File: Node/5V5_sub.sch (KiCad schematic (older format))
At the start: 21 parts, among them U501 TPS54361

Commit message: Generated BOM, filled out part numbers for precision resistors and headers.
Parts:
- R505: MFG. P/N (none) -> RC0805FR-0766K5L; Manufacturer (none) -> Yageo; Vendor (none) -> DigiKey; Vendor P/N (none) -> 311-66.5KCRCT-ND
- R508: MFG. P/N (none) -> RC0805FR-0711K3L; Manufacturer (none) -> Yageo; Vendor (none) -> DigiKey; Vendor P/N (none) -> 311-11.3KCRCT-ND
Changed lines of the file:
@@
 EESchema Schematic File Version 2
 LIBS:hyper_capstone
+LIBS:Connector
 LIBS:node-cache
 EELAYER 25 0
@@
 	3350 4650 3350 4850
 $Comp
-L GND #PWR510
+L GND #PWR034
 U 1 1 59F1BBFD
 P 3350 4850
-F 0 "#PWR510" H 3350 4600 60  0001 C CNN
+F 0 "#PWR034" H 3350 4600 60  0001 C CNN
 F 1 "GND" H 3350 4700 60  0000 C CNN
 F 2 "" H 3350 4850 60  0000 C CNN
@@
 	2850 4500 2850 4850
 $Comp
-L GND #PWR509
+L GND #PWR035
 U 1 1 59F1BC04
 P 2850 4850
-F 0 "#PWR509" H 2850 4600 60  0001 C CNN
+F 0 "#PWR035" H 2850 4600 60  0001 C CNN
 F 1 "GND" H 2850 4700 60  0000 C CNN
 F 2 "" H 2850 4850 60  0000 C CNN
@@
 Connection ~ 3800 5750
 $Comp
-L GND #PWR513
+L GND #PWR036
 U 1 1 59F1BC0B
 P 3800 5800
-F 0 "#PWR513" H 3800 5550 60  0001 C CNN
+F 0 "#PWR036" H 3800 5550 60  0001 C CNN
 F 1 "GND" H 3800 5650 60  0000 C CNN
 F 2 "" H 3800 5800 60  0000 C CNN
@@
 	5750 4300 5750 4450
 $Comp
-L GND #PWR502
+L GND #PWR037
 U 1 1 59F1BC3A
 P 5750 4450
-F 0 "#PWR502" H 5750 4200 60  0001 C CNN
+F 0 "#PWR037" H 5750 4200 60  0001 C CNN
 F 1 "GND" H 5750 4300 60  0000 C CNN
 F 2 "" H 5750 4450 60  0000 C CNN
@@
 	6250 4600 6250 4700
 $Comp
-L GND #PWR504
+L GND #PWR038
 U 1 1 59F1BC42
 P 6250 4700
-F 0 "#PWR504" H 6250 4450 60  0001 C CNN
+F 0 "#PWR038" H 6250 4450 60  0001 C CNN
 F 1 "GND" H 6250 4550 60  0000 C CNN
 F 2 "" H 6250 4700 60  0000 C CNN
@@
 F 2 "Resistors_SMD:R_0805_HandSoldering" V 7180 3950 30  0001 C CNN
 F 3 "" H 7250 3950 30  0000 C CNN
-F 4 "ERJ-6ENF6652V" H 7250 3950 60  0001 C CNN "Mfg. Part Num"
-F 5 "Panasonic" H 7250 3950 60  0001 C CNN "Mfg. Name"
-F 6 "P66.5KCCT-ND" H 7250 3950 60  0001 C CNN "Vendor Part Num"
-F 7 "Digi-Key" H 7250 3950 60  0001 C CNN "Vendor Name"
+F 4 "Yageo" H 7250 3950 60  0001 C CNN "Manufacturer"
+F 5 "RC0805FR-0766K5L" H 7250 3950 60  0001 C CNN "MFG. P/N"
+F 6 "DigiKey" H 7250 3950 60  0001 C CNN "Vendor"
+F 7 "311-66.5KCRCT-ND" H 7250 3950 60  0001 C CNN "Vendor P/N"
 F 8 "1%" H 7400 3900 60  0000 C CNN "Tolerance"
+F 9 "ERJ-6ENF6652V" H 7250 3950 60  0001 C CNN "Mfg. Part Num"
+F 10 "Panasonic" H 7250 3950 60  0001 C CNN "Mfg. Name"
+F 11 "P66.5KCCT-ND" H 7250 3950 60  0001 C CNN "Vendor Part Num"
+F 12 "Digi-Key" H 7250 3950 60  0001 C CNN "Vendor Name"
 	1    7250 3950
 	1    0    0    -1
@@
 Connection ~ 7250 4300
 $Comp
-L GND #PWR512
+L GND #PWR039
 U 1 1 59F1BC5A
 P 7250 5000
-F 0 "#PWR512" H 7250 4750 60  0001 C CNN
+F 0 "#PWR039" H 7250 4750 60  0001 C CNN
 F 1 "GND" H 7250 4850 60  0000 C CNN
 F 2 "" H 7250 5000 60  0000 C CNN
@@
 	7850 4100 7850 4250
 $Comp
-L GND #PWR501
+L GND #PWR040
 U 1 1 59F1BC6E
 P 7850 4250
-F 0 "#PWR501" H 7850 4000 60  0001 C CNN
+F 0 "#PWR040" H 7850 4000 60  0001 C CNN
 F 1 "GND" H 7850 4100 60  0000 C CNN
 F 2 "" H 7850 4250 60  0000 C CNN
@@
 	4900 4600 4900 4700
 $Comp
-L GND #PWR503
+L GND #PWR041
 U 1 1 59F1BC77
 P 4900 4700
-F 0 "#PWR503" H 4900 4450 60  0001 C CNN
+F 0 "#PWR041" H 4900 4450 60  0001 C CNN
 F 1 "GND" H 4900 4550 60  0000 C CNN
 F 2 "" H 4900 4700 60  0000 C CNN
@@
 	1950 4050 1950 4800
 $Comp
-L GND #PWR507
+L GND #PWR042
 U 1 1 59F1BC9B
 P 1950 4800
-F 0 "#PWR507" H 1950 4550 60  0001 C CNN
+F 0 "#PWR042" H 1950 4550 60  0001 C CNN
 F 1 "GND" H 1950 4650 60  0000 C CNN
 F 2 "" H 1950 4800 60  0000 C CNN
@@
 	9700 4400 9700 4700
 $Comp
-L GND #PWR506
+L GND #PWR043
 U 1 1 59F1BCD5
 P 9700 4700
-F 0 "#PWR506" H 9700 4450 60  0001 C CNN
+F 0 "#PWR043" H 9700 4450 60  0001 C CNN
 F 1 "GND" H 9700 4550 60  0000 C CNN
 F 2 "" H 9700 4700 60  0000 C CNN
@@
 	10350 4100 10350 4250
 $Comp
-L GND #PWR511
+L GND #PWR044
 U 1 1 59F1BCE0
 P 10350 4850
-F 0 "#PWR511" H 10350 4600 60  0001 C CNN
+F 0 "#PWR044" H 10350 4600 60  0001 C CNN
 F 1 "GND" H 10350 4700 60  0000 C CNN
 F 2 "" H 10350 4850 60  0000 C CNN
@@
 	2350 4050 2350 4800
 $Comp
-L GND #PWR508
+L GND #PWR045
 U 1 1 59F1CBAA
 P 2350 4800
-F 0 "#PWR508" H 2350 4550 60  0001 C CNN
+F 0 "#PWR045" H 2350 4550 60  0001 C CNN
 F 1 "GND" H 2350 4650 60  0000 C CNN
 F 2 "" H 2350 4800 60  0000 C CNN
@@
 F 2 "Resistors_SMD:R_0805_HandSoldering" V 7180 4650 30  0001 C CNN
 F 3 "" H 7250 4650 30  0000 C CNN
-F 4 "Digi-Key" H 7250 4650 60  0001 C CNN "Vendor Name"
-F 5 "1%" H 7400 4600 60  0000 C CNN "Tolerance"
+F 4 "Yageo" H 7250 4650 60  0001 C CNN "Manufacturer"
+F 5 "RC0805FR-0711K3L" H 7250 4650 60  0001 C CNN "MFG. P/N"
+F 6 "DigiKey" H 7250 4650 60  0001 C CNN "Vendor"
+F 7 "311-11.3KCRCT-ND" H 7250 4650 60  0001 C CNN "Vendor P/N"
+F 8 "1%" H 7400 4600 60  0000 C CNN "Tolerance"
+F 9 "Digi-Key" H 7250 4650 60  0001 C CNN "Vendor Name"
 	1    7250 4650
 	1    0    0    -1
@@
 	9200 4350 9200 4700
 $Comp
-L GND #PWR505
+L GND #PWR046
 U 1 1 5A1A8A0F
 P 9200 4700
-F 0 "#PWR505" H 9200 4450 60  0001 C CNN
+F 0 "#PWR046" H 9200 4450 60  0001 C CNN
 F 1 "GND" H 9200 4550 60  0000 C CNN
 F 2 "" H 9200 4700 60  0000 C CNN

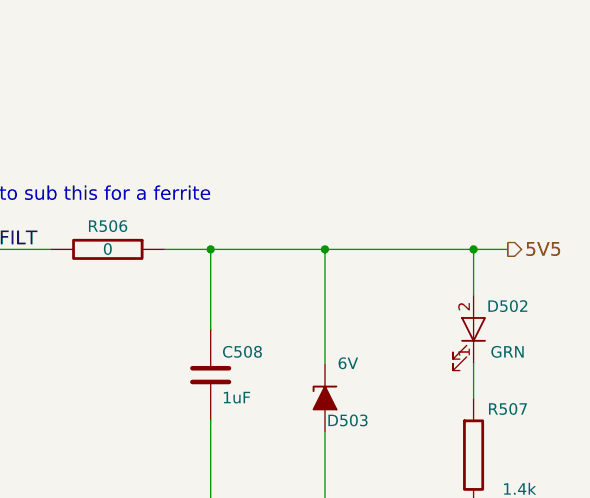
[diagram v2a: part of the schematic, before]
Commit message: Added testpoints and silkscreen descriptions to PCB. Added Paradigm template to schematic.
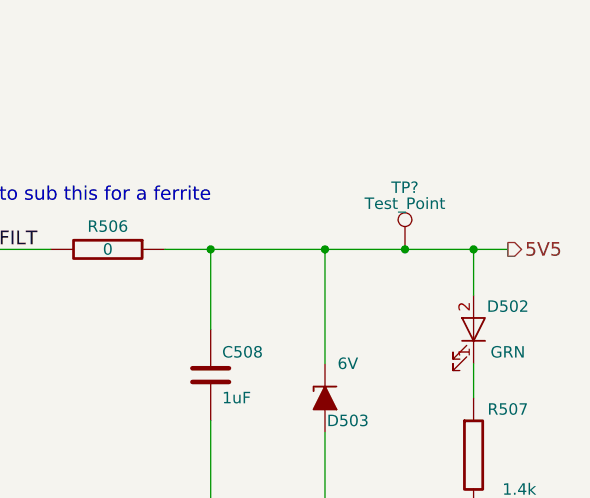
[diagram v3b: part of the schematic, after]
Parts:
- added TP?: Test_Point, Measurement_Points:Test_Point_Keystone_5000-5004_Miniature, symbol Test_Point
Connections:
- net 5V5: now also TP?.1
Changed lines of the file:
@@
 encoding utf-8
 Sheet 5 22
-Title ""
+Title "Node Board"
 Date ""
-Rev ""
+Rev "Rev 1.0"
 Comp ""
 Comment1 ""
@@
 Text Label 3550 2700 0    60   ~ 0
 ENABLE
+$Comp
+L Test_Point TP?
+U 1 1 5A71E940
+P 10050 3600
+F 0 "TP?" H 10050 3870 50  0000 C CNN
+F 1 "Test_Point" H 10050 3800 50  0000 C CNN
+F 2 "Measurement_Points:Test_Point_Keystone_5000-5004_Miniature" H 10250 3600 50  0001 C CNN
+F 3 "" H 10250 3600 50  0001 C CNN
+F 4 "Keystone Electronics" H 10050 3600 60  0001 C CNN "Manufacturer"
+F 5 "5000" H 10050 3600 60  0001 C CNN "Manufacturer P/N"
+F 6 "DigiKey" H 10050 3600 60  0001 C CNN "Vendor"
+F 7 "36-5000-ND" H 10050 3600 60  0001 C CNN "Vendor P/N"
+	1    10050 3600
+	1    0    0    -1
+$EndComp
+Connection ~ 10050 3600
 $EndSCHEMATC

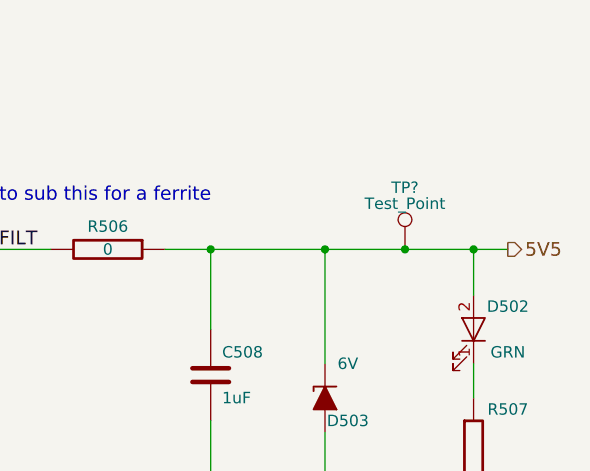
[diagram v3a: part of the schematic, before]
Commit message: fixed and routed driver spi issue
Added new rx/tx bus for solenoid driver. Routed it too. Nice.
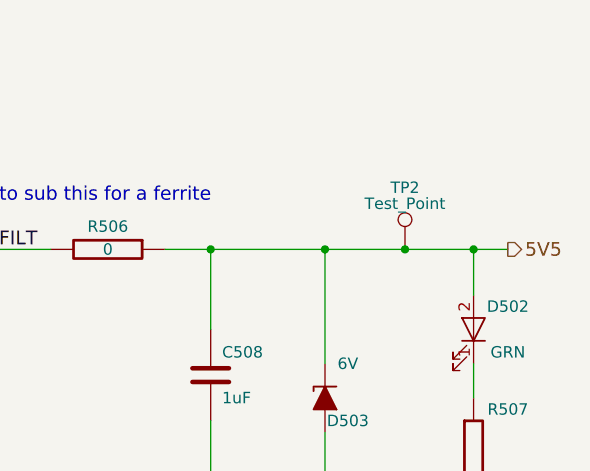
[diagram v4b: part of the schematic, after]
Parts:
- gave numbers to parts that had none: 1
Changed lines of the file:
@@
 EESchema Schematic File Version 2
 LIBS:hyper_capstone
-LIBS:Connector
 LIBS:node-cache
 EELAYER 25 0
@@
 ENABLE
 $Comp
-L Test_Point TP?
+L Test_Point TP2
 U 1 1 5A71E940
 P 10050 3600
-F 0 "TP?" H 10050 3870 50  0000 C CNN
+F 0 "TP2" H 10050 3870 50  0000 C CNN
 F 1 "Test_Point" H 10050 3800 50  0000 C CNN
 F 2 "Measurement_Points:Test_Point_Keystone_5000-5004_Miniature" H 10250 3600 50  0001 C CNN

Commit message: Updated bom stuff, made new gerbers and added a trace route
damn,
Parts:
- C501, C502: Mfg. Part Num C2012X7R1H225K125AC -> CGA4J1X7R1V225K125AE
- C505: Mfg. Part Num C0805C100K5GACTU -> C0805C100JDGACTU; Vendor Part Num 399-7975-1-ND -> 399-7062-1-ND
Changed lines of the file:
@@
 $EndComp
 Wire Wire Line
-	4200 4300 3800 4300
+	3800 4300 4200 4300
 Wire Wire Line
 	3800 4300 3800 4700
@@
 F 2 "Capacitors_SMD:C_0805_HandSoldering" H 4288 5300 30  0001 C CNN
 F 3 "" H 4250 5450 60  0000 C CNN
-F 4 "C0805C100K5GACTU" H 4250 5450 60  0001 C CNN "Mfg. Part Num"
+F 4 "C0805C100JDGACTU" H 4250 5450 60  0001 C CNN "Mfg. Part Num"
 F 5 "Kemet" H 4250 5450 60  0001 C CNN "Mfg. Name"
-F 6 "399-7975-1-ND" H 4250 5450 60  0001 C CNN "Vendor Part Num"
+F 6 "399-7062-1-ND" H 4250 5450 60  0001 C CNN "Vendor Part Num"
 F 7 "Digi-Key" H 4250 5450 60  0001 C CNN "Vendor Name"
 	1    4250 5450
@@
 F 2 "Capacitors_SMD:C_0805_HandSoldering" H 1988 3700 30  0001 C CNN
 F 3 "" H 1950 3850 60  0000 C CNN
-F 4 "C2012X7R1H225K125AC" H 1950 3850 60  0001 C CNN "Mfg. Part Num"
+F 4 "CGA4J1X7R1V225K125AE" H 1950 3850 60  0001 C CNN "Mfg. Part Num"
 F 5 "TDK" H 1950 3850 60  0001 C CNN "Mfg. Name"
 F 6 "445-5968-1-ND" H 1950 3850 60  0001 C CNN "Vendor Part Num"
@@
 Text Notes 7850 3400 0    60   ~ 0
 May want to sub this for a ferrite
-$Comp
-L C_large C502
-U 1 1 5A1A604D
-P 2350 3850
-F 0 "C502" H 2400 3950 50  0000 L CNN
-F 1 "2.2uF" H 2400 3750 50  0000 L CNN
-F 2 "Capacitors_SMD:C_0805_HandSoldering" H 2388 3700 30  0001 C CNN
-F 3 "" H 2350 3850 60  0000 C CNN
-F 4 "C2012X7R1H225K125AC" H 2350 3850 60  0001 C CNN "Mfg. Part Num"
-F 5 "TDK" H 2350 3850 60  0001 C CNN "Mfg. Name"
-F 6 "445-5968-1-ND" H 2350 3850 60  0001 C CNN "Vendor Part Num"
-F 7 "Digi-Key" H 2350 3850 60  0001 C CNN "Vendor Name"
-	1    2350 3850
-	1    0    0    -1
-$EndComp
 Text Label 2550 3500 0    60   ~ 0
 24V0_R
@@
 $EndComp
 Connection ~ 10050 3600
+$Comp
+L C_large C502
+U 1 1 5B528C29
+P 2350 3850
+F 0 "C502" H 2400 3950 50  0000 L CNN
+F 1 "2.2uF" H 2400 3750 50  0000 L CNN
+F 2 "Capacitors_SMD:C_0805_HandSoldering" H 2388 3700 30  0001 C CNN
+F 3 "" H 2350 3850 60  0000 C CNN
+F 4 "CGA4J1X7R1V225K125AE" H 2350 3850 60  0001 C CNN "Mfg. Part Num"
+F 5 "TDK" H 2350 3850 60  0001 C CNN "Mfg. Name"
+F 6 "445-5968-1-ND" H 2350 3850 60  0001 C CNN "Vendor Part Num"
+F 7 "Digi-Key" H 2350 3850 60  0001 C CNN "Vendor Name"
+	1    2350 3850
+	1    0    0    -1
+$EndComp
 $EndSCHEMATC

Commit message: Added ADC
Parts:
- C501, C502, C503, C504, C505, C506, C507, C508: symbol C_large -> node-rescue:C_large
- D501: symbol DIODESCH -> node-rescue:DIODESCH
- D502: symbol LED -> node-rescue:LED
- D503: symbol D_Zener_ALT -> node-rescue:D_Zener_ALT
- L501: symbol L_large -> node-rescue:L_large
- R501, R502, R503, R504, R505, R506, R507, R508: symbol R_large -> node-rescue:R_large
- TP2: symbol Test_Point -> node-rescue:Test_Point
- U501: symbol TPS54361 -> node-rescue:TPS54361
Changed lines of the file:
@@
-EESchema Schematic File Version 2
-LIBS:hyper_capstone
+EESchema Schematic File Version 4
 LIBS:node-cache
-EELAYER 25 0
+EELAYER 26 0
 EELAYER END
 $Descr A4 11693 8268
@@
 ENABLE
 $Comp
-L TPS54361 U501
+L node-rescue:TPS54361 U501
 U 1 1 59F1BB94
 P 4850 3950
@@
 $EndComp
 $Comp
-L R_large R501
+L node-rescue:R_large R501
 U 1 1 59F1BB9F
 P 1500 3500
@@
 	1750 3500 4200 3500
 $Comp
-L R_large R503
+L node-rescue:R_large R503
 U 1 1 59F1BBAC
 P 3650 3700
@@
 	2850 3900 2850 4000
 $Comp
-L R_large R502
+L node-rescue:R_large R502
 U 1 1 59F1BBBD
 P 2850 4250
@@
 	3350 4100 3350 4250
 $Comp
-L C_large C503
+L node-rescue:C_large C503
 U 1 1 59F1BBCA
 P 3350 4450
@@
 	3800 4300 3800 4700
 $Comp
-L C_large C504
+L node-rescue:C_large C504
 U 1 1 59F1BBD7
 P 3800 4900
@@
 $EndComp
 $Comp
-L R_large R504
+L node-rescue:R_large R504
 U 1 1 59F1BBE2
 P 4250 4900
@@
 $EndComp
 $Comp
-L C_large C505
+L node-rescue:C_large C505
 U 1 1 59F1BBED
 P 4250 5450
@@
 	3350 4650 3350 4850
 $Comp
-L GND #PWR034
+L node-rescue:GND #PWR034
 U 1 1 59F1BBFD
 P 3350 4850
@@
 	2850 4500 2850 4850
 $Comp
-L GND #PWR035
+L node-rescue:GND #PWR035
 U 1 1 59F1BC04
 P 2850 4850
@@
 Connection ~ 3800 5750
 $Comp
-L GND #PWR036
+L node-rescue:GND #PWR036
 U 1 1 59F1BC0B
 P 3800 5800
@@
 $EndComp
 $Comp
-L C_large C506
+L node-rescue:C_large C506
 U 1 1 59F1BC15
 P 6000 3600
@@
 	6250 3600 6250 4200
 $Comp
-L L_large L501
+L node-rescue:L_large L501
 U 1 1 59F1BC26
 P 6700 3600
@@
 $EndComp
 $Comp
-L DIODESCH D501
+L node-rescue:DIODESCH D501
 U 1 1 59F1BC31
 P 6250 4400
@@
 	5750 4300 5750 4450
 $Comp
-L GND #PWR037
+L node-rescue:GND #PWR037
 U 1 1 59F1BC3A
 P 5750 4450
@@
 	6250 4600 6250 4700
 $Comp
-L GND #PWR038
+L node-rescue:GND #PWR038
 U 1 1 59F1BC42
 P 6250 4700
@@
 Connection ~ 6250 3600
 $Comp
-L R_large R505
+L node-rescue:R_large R505
 U 1 1 59F1BC4D
 P 7250 3950
@@
 Connection ~ 7250 4300
 $Comp
-L GND #PWR039
+L node-rescue:GND #PWR039
 U 1 1 59F1BC5A
 P 7250 5000
@@
 $EndComp
 $Comp
-L C_large C507
+L node-rescue:C_large C507
 U 1 1 59F1BC64
 P 7850 3900
@@
 	7850 4100 7850 4250
 $Comp
-L GND #PWR040
+L node-rescue:GND #PWR040
 U 1 1 59F1BC6E
 P 7850 4250
@@
 	4900 4600 4900 4700
 $Comp
-L GND #PWR041
+L node-rescue:GND #PWR041
 U 1 1 59F1BC77
 P 4900 4700
@@
 $EndComp
 $Comp
-L C_large C501
+L node-rescue:C_large C501
 U 1 1 59F1BC91
 P 1950 3850
@@
 	1950 4050 1950 4800
 $Comp
-L GND #PWR042
+L node-rescue:GND #PWR042
 U 1 1 59F1BC9B
 P 1950 4800
@@
 $EndComp
 $Comp
-L D_Zener_ALT D503
+L node-rescue:D_Zener_ALT D503
 U 1 1 59F1BCB6
 P 9700 4250
@@
 $EndComp
 $Comp
-L R_large R507
+L node-rescue:R_large R507
 U 1 1 59F1BCC4
 P 10350 4500
@@
 	9700 4400 9700 4700
 $Comp
-L GND #PWR043
+L node-rescue:GND #PWR043
 U 1 1 59F1BCD5
 P 9700 4700
@@
 	10350 4100 10350 4250
 $Comp
-L GND #PWR044
+L node-rescue:GND #PWR044
 U 1 1 59F1BCE0
 P 10350 4850
@@
 	2350 4050 2350 4800
 $Comp
-L GND #PWR045
+L node-rescue:GND #PWR045
 U 1 1 59F1CBAA
 P 2350 4800
@@
 	10350 4750 10350 4850
 $Comp
-L LED D502
+L node-rescue:LED D502
 U 1 1 59F25D8B
 P 10350 3950
@@
 	9000 3600 10500 3600
 $Comp
-L R_large R508
+L node-rescue:R_large R508
 U 1 1 5A10B1CD
 P 7250 4650
@@
 	7250 4900 7250 5000
 $Comp
-L R_large R506
+L node-rescue:R_large R506
 U 1 1 5A0E1EE6
 P 8750 3600
@@
 5V5_UNFILT
 $Comp
-L C_large C508
+L node-rescue:C_large C508
 U 1 1 5A1A8886
 P 9200 4150
@@
 	9200 4350 9200 4700
 $Comp
-L GND #PWR046
+L node-rescue:GND #PWR046
 U 1 1 5A1A8A0F
 P 9200 4700
@@
 ENABLE
 $Comp
-L Test_Point TP2
+L node-rescue:Test_Point TP2
 U 1 1 5A71E940
 P 10050 3600
@@
 Connection ~ 10050 3600
 $Comp
-L C_large C502
+L node-rescue:C_large C502
 U 1 1 5B528C29
 P 2350 3850
